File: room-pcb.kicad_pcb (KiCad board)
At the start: 4 copper layers, 50 x 50 mm, 25 parts, among them J2 Conn_01x02, J3 Conn_01x04, J4 Conn_01x05, U1 COZIR, U2 BH1750FVI-TR, U3 AHT20, U5 ESP32-C6_SUPERMINI_TH

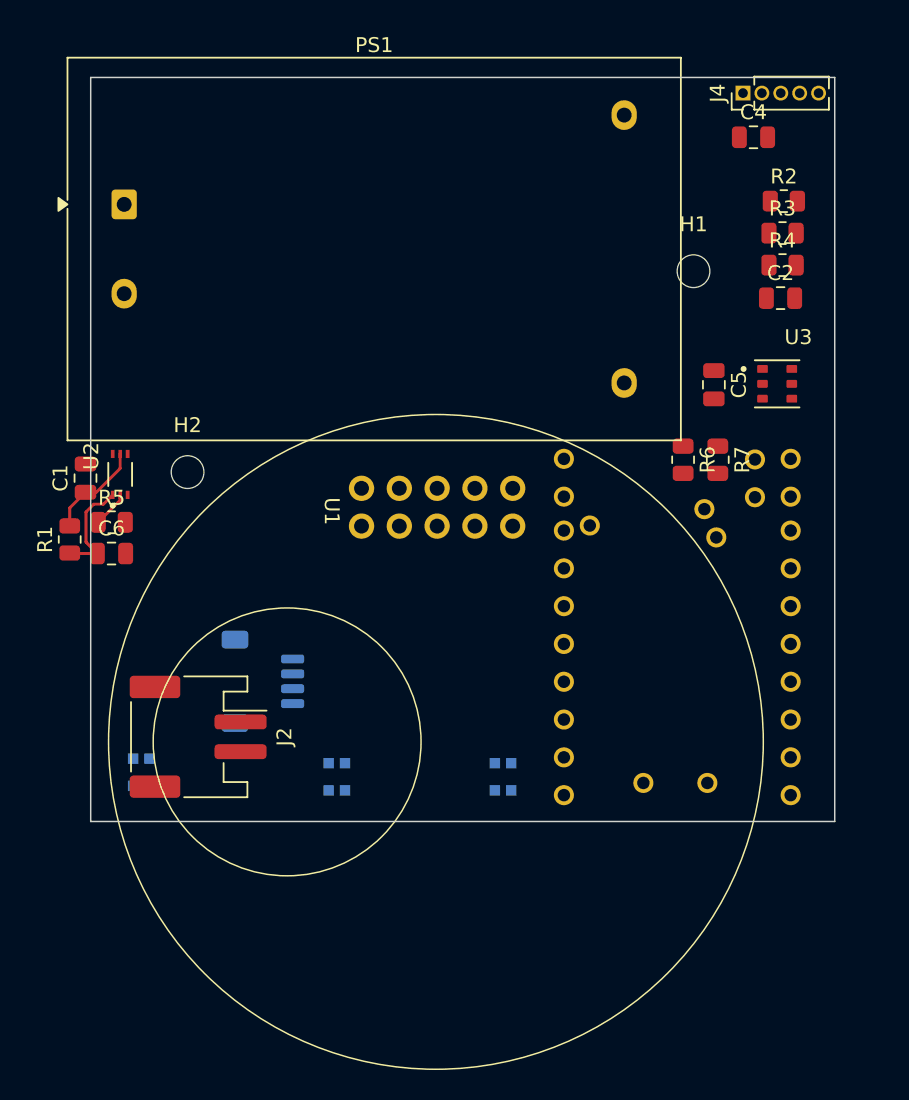
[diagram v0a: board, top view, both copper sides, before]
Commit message: first order with cozir fix and i2c fix
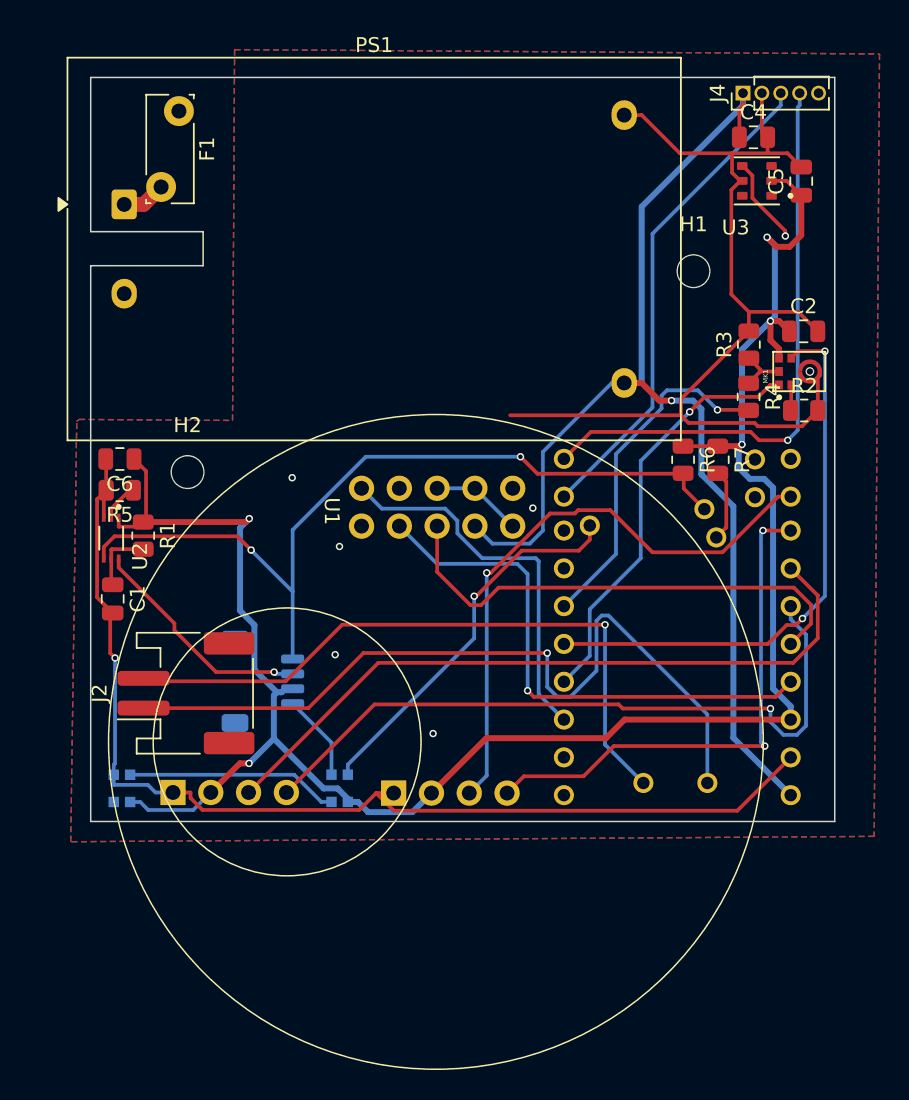
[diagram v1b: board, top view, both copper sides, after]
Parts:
- removed D3: WS2812B, LED_SMD:LED_WS2812B-2020_PLCC4_2.0x2.0mm
- added F1: Polyfuse, Fuse:Fuse_Bourns_MF-RG300, F.Cu at (105.4, 81.4)
- added J5: Conn_01x04, Connector_PinHeader_2.54mm:PinHeader_1x04_P2.54mm_Vertical, B.Cu at (119.8, 127.2)
- added J6: Conn_01x04, Connector_PinHeader_2.54mm:PinHeader_1x04_P2.54mm_Vertical, B.Cu at (105.0, 127.2)
- added MK1: ICS-43434, ICS-43434:MIC_ICS-43434, F.Cu at (147.1, 98.9)
- moved C5 14.9 mm to (147.2, 86.1), turned to 90 degrees
- moved D2 14.5 mm to (101.6, 126.9)
- moved R2 14.1 mm to (147.4, 101.5)
- moved U3 13.7 mm to (144.3, 86.1), turned to 180 degrees
- moved D1 11.0 mm to (116.2, 126.9)
- moved R4 9.14 mm to (143.7, 100.6), turned to -90 degrees
- moved C1 8.32 mm to (101.0, 114.2), turned to -90 degrees
- moved R3 7.83 mm to (143.7, 97.1), turned to 90 degrees
- moved C6 6.38 mm to (101.5, 104.8), turned to 180 degrees
- moved R1 4.95 mm to (103.0, 110.0), turned to -90 degrees
- moved U2 4.33 mm to (100.9, 110.1), turned to -90 degrees
- moved J2 3.04 mm to (105.9, 120.5), turned to 90 degrees
- moved C2 2.72 mm to (147.4, 96.2)
- moved R5 2.22 mm to (101.4, 106.9), turned to 180 degrees
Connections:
- D2 pad 2: Net-(D2-DOUT) -> unconnected-(D2-DOUT-Pad2)
- PS1 pad 1: unconnected-(PS1-AC/L-Pad1) -> Net-(PS1-AC/L)
- U5 pad 12: SCL -> unconnected-(U5-GPIO12-Pad12)
- U5 pad 13: SDA -> unconnected-(U5-GPIO13-Pad13)
- U5 pad 14: unconnected-(U5-GPIO14-Pad14) -> EX2
- U5 pad 15: unconnected-(U5-GPIO15-Pad15) -> EX3
- U5 pad 18: unconnected-(U5-GPIO18-Pad18) -> EX4
- U5 pad 21: unconnected-(U5-GPIO21-Pad21) -> SCL
- U5 pad 22: unconnected-(U5-GPIO22-Pad22) -> SDA
- U5 pad 8: CS -> unconnected-(U5-GPIO8-Pad8)
- U5 pad 9: unconnected-(U5-GPIO9-Pad9) -> EX1
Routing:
- net GND: track 0.00 -> 154.2 mm, vias 0 -> 6
- net +3.3V: track 7.25 -> 135.1 mm, vias 0 -> 5
- net VCC: track 0.00 -> 79.3 mm, vias 0 -> 1
- net SDA: track 0.00 -> 61.7 mm, vias 0 -> 3
- net BAT+: track 0.00 -> 53.6 mm, vias 0 -> 1
- net EX3: track 0.00 -> 48.0 mm
- net EX4: track 0.00 -> 47.5 mm, vias 0 -> 1
- net BAT-: track 0.00 -> 44.4 mm, vias 0 -> 1
- net EX1: track 0.00 -> 40.2 mm, vias 0 -> 1
- net TX1: track 0.00 -> 39.7 mm, vias 0 -> 1
- net CLK: track 0.00 -> 37.8 mm, vias 0 -> 2
- net TX: track 0.00 -> 36.1 mm, vias 0 -> 1
- net EX2: track 0.00 -> 35.1 mm, vias 0 -> 2
- net RX: track 0.00 -> 33.3 mm
- net RX1: track 0.00 -> 33.2 mm
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- added copper zone on B.Cu, net GND
- added copper zone on F.Cu, net GND
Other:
- outline, holes or cut-outs redrawn
- copper layers 4 -> 2
- board text added: "Dat is wat waard, wat jij wil Jerry ;)"
